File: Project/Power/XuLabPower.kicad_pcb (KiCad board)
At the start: 8 copper layers, 74 x 147 mm, 179 parts, among them J1 Servo, J10 Battery, J11 Battery, J12 Battery, J13 I2C, J14 SWD, J15 SPI1, J16 5V_2A, J17 5V_6A, J2 Servo, J3 Servo, J4 Servo, J5 Servo, J6 Servo, J7 Servo, J8 Servo, J9 Battery, Q1 SQJ138ELP, Q2 SQJ138ELP, Q3 SQJ138ELP, Q4 SQJ138ELP, Q5 SQJ138ELP, Q6 SQJ138ELP, SW1 SW_Push, U1 LM74502, U10 INA199B3DCKR, U11 TL331, U12 INA199B3DCKR, U13 TL331, U14 STM32L422KBTx, U15 TPS560200, U16 MIC5219-3.3YM5, U17 TPS562200, U18 TPS54627, U19 INA226, U2 NCV68061, U20 INA226, U21 INA226, U22 INA226, U23 INA226, U24 INA226, U25 INA226, U26 INA226, U3 NCV68061, U4 INA199B3DCKR, U5 TL331, U6 INA199B3DCKR, U7 TL331, U8 NCV68061, U9 NCV68061

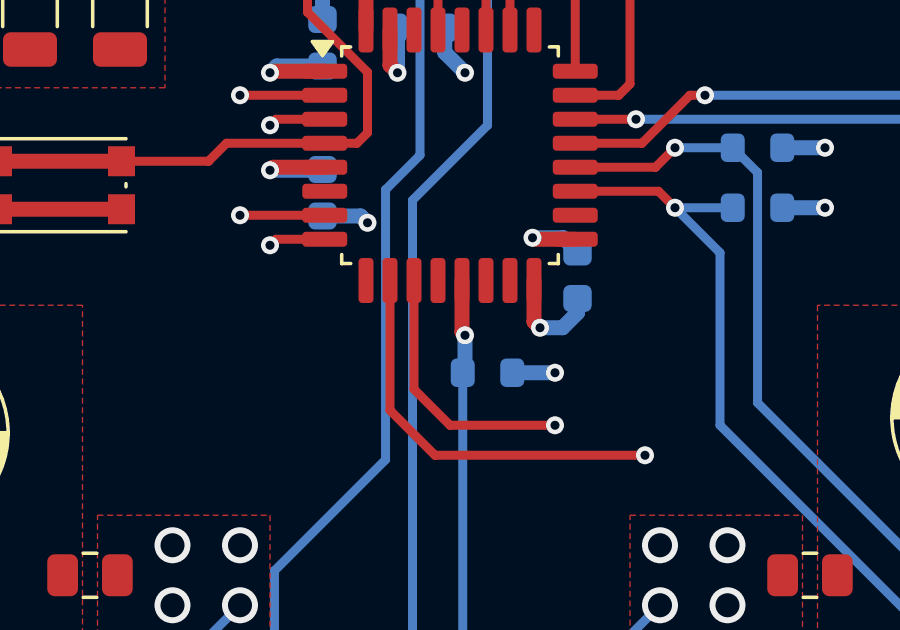
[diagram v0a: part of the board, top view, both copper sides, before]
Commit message: Add LEDs to the microcontroller
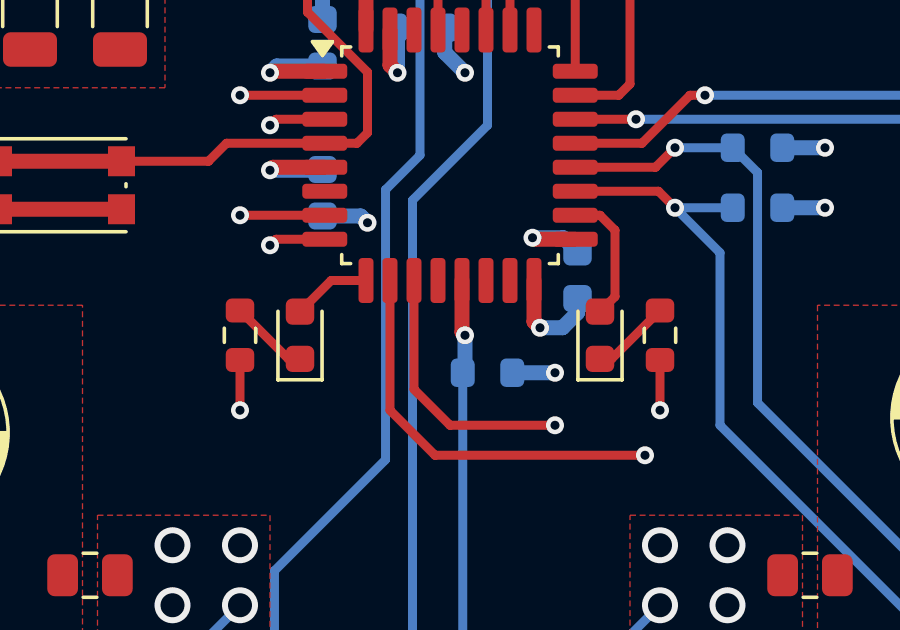
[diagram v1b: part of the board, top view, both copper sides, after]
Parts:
- added D10: Green, LED_SMD:LED_0603_1608Metric, F.Cu at (153.0, 53.0)
- added D9: Amber, LED_SMD:LED_0603_1608Metric, F.Cu at (143.0, 53.0)
- added R45: 330, Resistor_SMD:R_0603_1608Metric, F.Cu at (141.0, 53.0)
- added R46: 330, Resistor_SMD:R_0603_1608Metric, F.Cu at (155.0, 53.0)
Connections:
- U14 pad 18: unconnected-(U14-PA8-Pad18) -> /Microcontroller/LED_OUT2
- U14 pad 9: unconnected-(U14-PA3-Pad9) -> /Microcontroller/LED_OUT1
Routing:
- net /Microcontroller/LED_OUT2: track 0.00 -> 4.45 mm
- net GND: track 195.4 -> 198.7 mm, vias 89 -> 91
- net Net-(D9-K): track 0.00 -> 2.67 mm
- net Net-(D10-K): track 0.00 -> 2.67 mm
- net /Microcontroller/LED_OUT1: track 0.00 -> 2.63 mm

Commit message: Add stitching vias
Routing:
- net GND: vias 91 -> 138

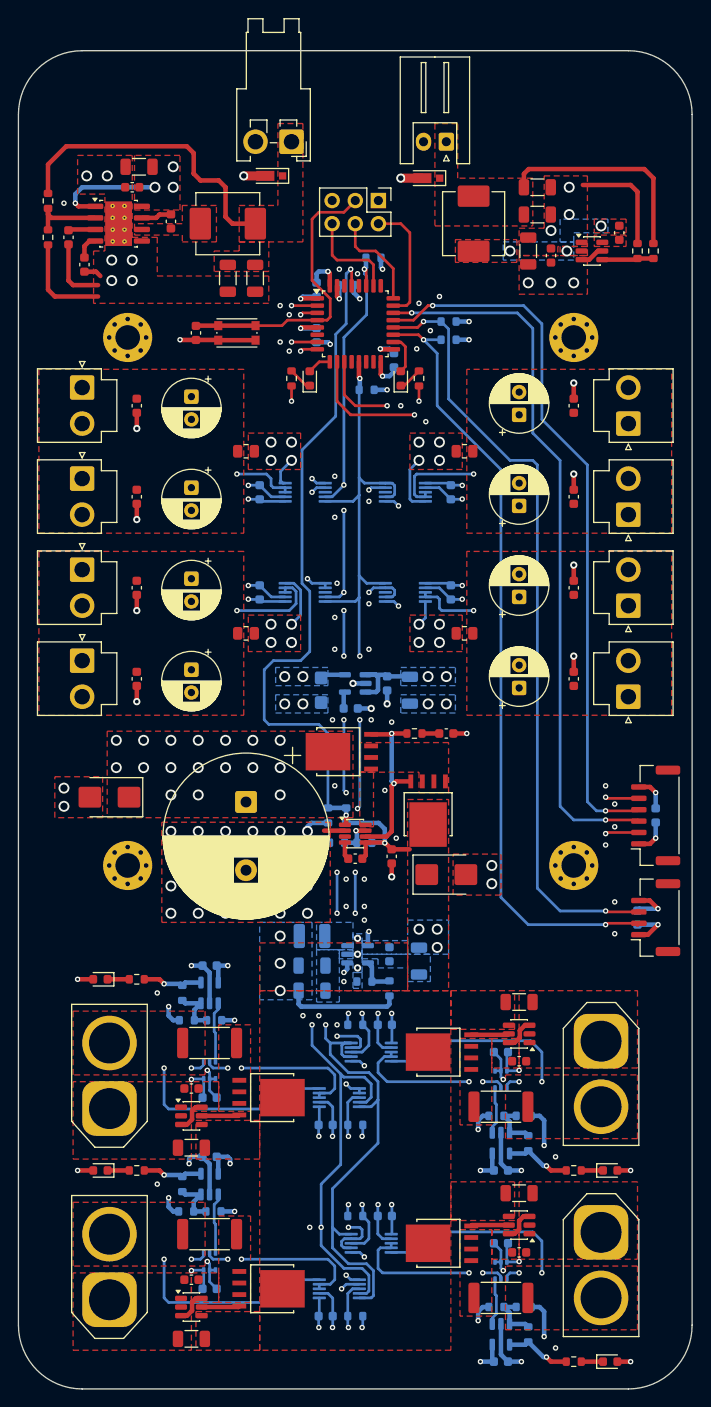
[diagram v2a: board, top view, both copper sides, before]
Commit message: Add silkscreen
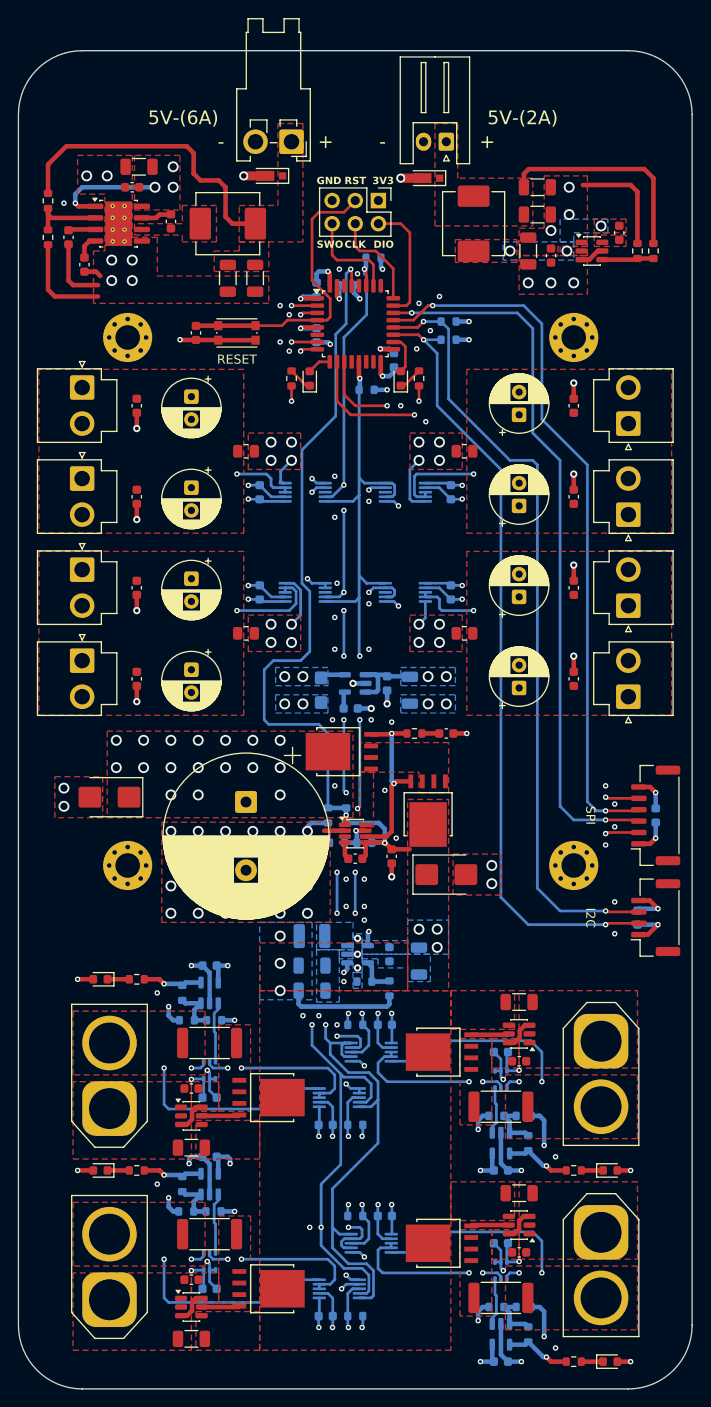
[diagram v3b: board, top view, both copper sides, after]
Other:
- board text added: "+"
- board text added: "-"
- board text added: "3V3"
- board text added: "5V-(2A)"
- board text added: "5V-(6A)"
- board text added: "CLK"
- board text added: "DIO"
- board text added: "Designed By: Owen Allison 03/2026 - Rev B"
- board text added: "GND"
- board text added: "I2C"
- board text added: "RESET"
- board text added: "RST"
- board text added: "SPI"
- board text added: "SWO"
- board text added: "Team 29: Owen Allison Jose Cabrera Sean Curry Alex Hansen Anthony Javier Topher Prokopius Ilsa Runge Leon Steinbach Carter Winkleman"
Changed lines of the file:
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@@
 		(layer "Edge.Cuts")
+	)
+	(gr_text "5V-(6A)"
+		(at 133 23.5 0)
+		(layer "F.SilkS")
+		(effects
+			(font
+				(size 1.5 1.5)
+				(thickness 0.2)
+			)
+			(justify right top)
+		)
+	)
+	(gr_text "+"
+		(at 162.5 27 0)
+		(layer "F.SilkS")
+		(effects
+			(font
+				(size 1.5 1.5)
+				(thickness 0.2)
+			)
+		)
+	)
+	(gr_text "SWO"
+		(at 143.75 38.75 0)
+		(layer "F.SilkS")
+		(effects
+			(font
+				(size 0.8 0.8)
+				(thickness 0.15)
+				(bold yes)
+			)
+			(justify left bottom)
+		)
+	)
+	(gr_text "-"
+		(at 151 27 0)
+		(layer "F.SilkS")
+		(effects
+			(font
+				(size 1.5 1.5)
+				(thickness 0.2)
+			)
+		)
+	)
+	(gr_text "3V3"
+		(at 152.25 31.75 0)
+		(layer "F.SilkS")
+		(effects
+			(font
+				(size 0.8 0.8)
+				(thickness 0.15)
+				(bold yes)
+			)
+			(justify right bottom)
+		)
+	)
+	(gr_text "SPI"
+		(at 173.25 101 270)
+		(layer "F.SilkS")
+		(effects
+			(font
+				(size 1 1)
+				(thickness 0.15)
+			)
+			(justify bottom)
+		)
+	)
+	(gr_text "I2C"
+		(at 173.25 112.25 270)
+		(layer "F.SilkS")
+		(effects
+			(font
+				(size 1 1)
+				(thickness 0.15)
+			)
+			(justify bottom)
+		)
+	)
+	(gr_text "5V-(2A)"
+		(at 162.5 23.5 0)
+		(layer "F.SilkS")
+		(effects
+			(font
+				(size 1.5 1.5)
+				(thickness 0.2)
+			)
+			(justify left top)
+		)
+	)
+	(gr_text "-"
+		(at 133.25 27 0)
+		(layer "F.SilkS")
+		(effects
+			(font
+				(size 1.5 1.5)
+				(thickness 0.2)
+			)
+		)
+	)
+	(gr_text "+"
+		(at 144.75 27 0)
+		(layer "F.SilkS")
+		(effects
+			(font
+				(size 1.5 1.5)
+				(thickness 0.2)
+			)
+		)
+	)
+	(gr_text "GND"
+		(at 143.75 31.75 0)
+		(layer "F.SilkS")
+		(effects
+			(font
+				(size 0.8 0.8)
+				(thickness 0.15)
+				(bold yes)
+			)
+			(justify left bottom)
+		)
+	)
+	(gr_text "RST"
+		(at 148 31.75 0)
+		(layer "F.SilkS")
+		(effects
+			(font
+				(size 0.8 0.8)
+				(thickness 0.15)
+				(bold yes)
+			)
+			(justify bottom)
+		)
+	)
+	(gr_text "CLK"
+		(at 148 38.75 0)
+		(layer "F.SilkS")
+		(effects
+			(font
+				(size 0.8 0.8)
+				(thickness 0.15)
+				(bold yes)
+			)
+			(justify bottom)
+		)
+	)
+	(gr_text "DIO"
+		(at 152.25 38.75 0)
+		(layer "F.SilkS")
+		(effects
+			(font
+				(size 0.8 0.8)
+				(thickness 0.15)
+				(bold yes)
+			)
+			(justify right bottom)
+		)
+	)
+	(gr_text "RESET"
+		(at 135 51.5 0)
+		(layer "F.SilkS")
+		(effects
+			(font
+				(size 1 1)
+				(thickness 0.15)
+			)
+			(justify bottom)
+		)
+	)
+	(gr_text "Team 29:\nOwen Allison\n\nJose Cabrera\n\nSean Curry\n\nAlex Hansen\n\nAnthony Javier\n\nTopher Prokopius\n\nIlsa Runge\n\nLeon Steinbach\n\nCarter Winkleman"
+		(at 137.5 34.5 0)
+		(layer "B.SilkS")
+		(effects
+			(font
+				(size 1 1)
+				(thickness 0.15)
+			)
+			(justify left top mirror)
+		)
+	)
+	(gr_text "Designed By: Owen Allison\n03/2026 - Rev B"
+		(at 179.75 28.5 0)
+		(layer "B.SilkS")
+		(effects
+			(font
+				(size 1 1)
+				(thickness 0.15)
+			)
+			(justify left top mirror)
+		)
 	)
 	(segment
